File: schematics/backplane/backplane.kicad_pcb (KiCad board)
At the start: 4 copper layers, 91 x 95.3 mm, 8 parts

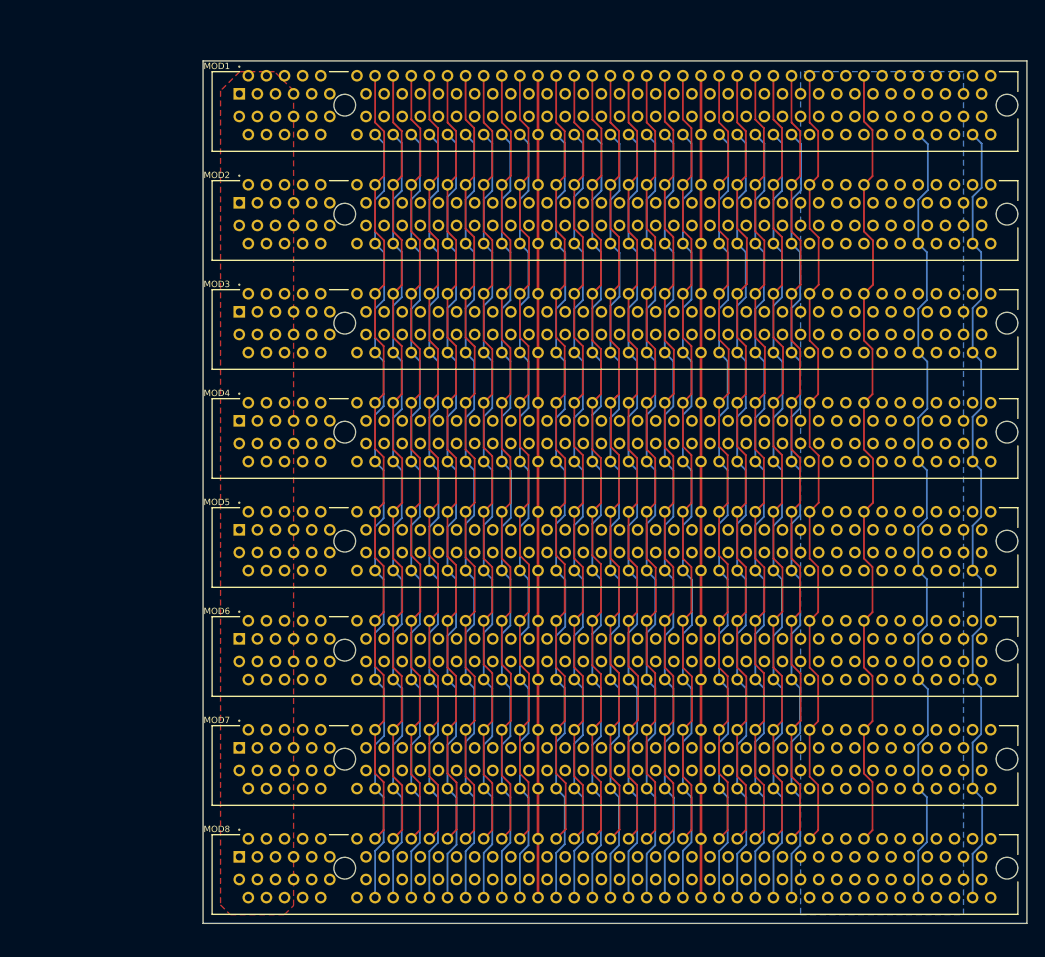
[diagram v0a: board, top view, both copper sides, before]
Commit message: Update backplane, add power supply and debug port
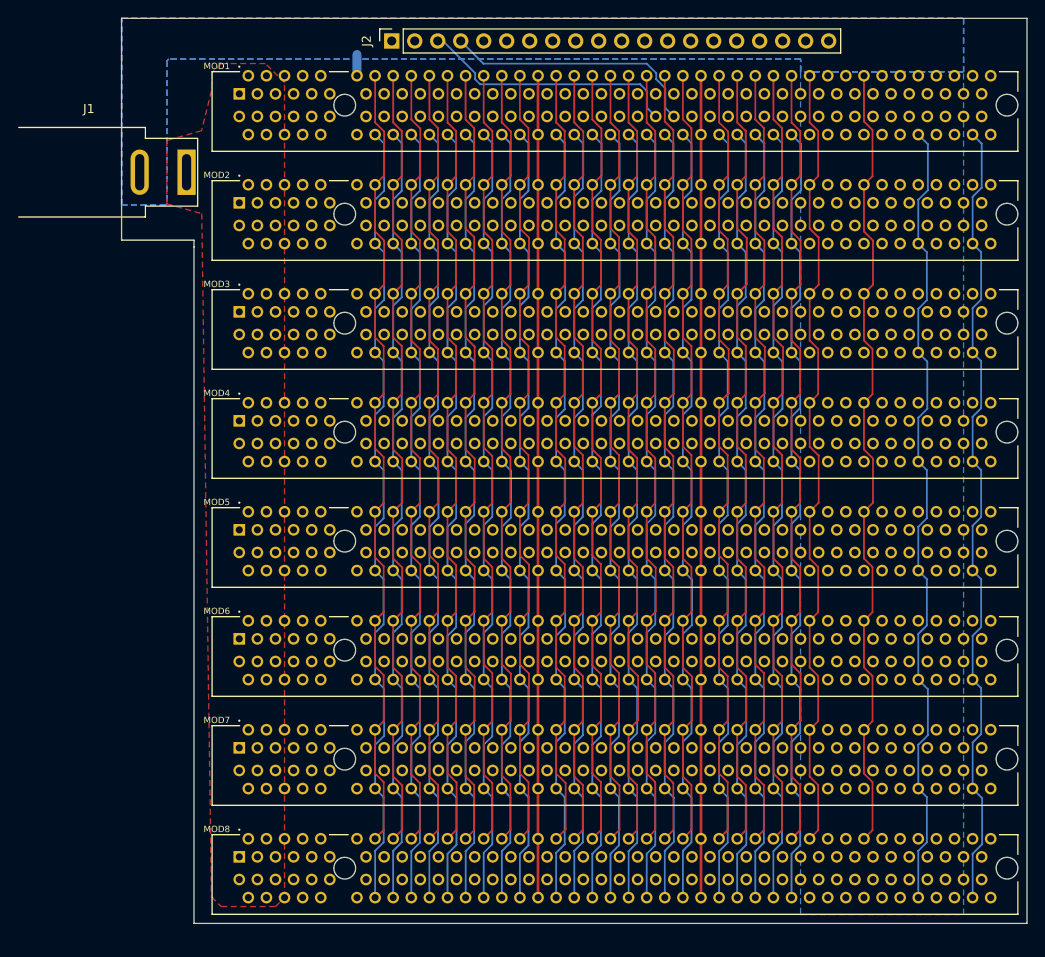
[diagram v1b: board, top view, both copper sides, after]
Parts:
- added J1: Conn_01x02, Connector_BarrelJack:BarrelJack_SwitchcraftConxall_RAPC10U_Horizontal, F.Cu at (74.2, 42.0)
- added J2: Conn_01x20, Connector_PinSocket_2.54mm:PinSocket_1x20_P2.54mm_Vertical, F.Cu at (96.8, 27.5)
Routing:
- net /~{SCCLR}: track 90.0 -> 119.0 mm
- net /PCINC: track 89.9 -> 118.6 mm
- net /STATE8: track 89.9 -> 108.9 mm
- net /STATE9: track 89.9 -> 108.1 mm
- net /STATE11: track 89.8 -> 105.0 mm
- net /STATE10: track 89.8 -> 104.3 mm
- net /STATE12: track 89.8 -> 101.2 mm
- net /STATE13: track 89.9 -> 101.3 mm
- net /STATE15: track 89.8 -> 98.2 mm
- net /STATE14: track 89.8 -> 98.2 mm
- net /DATA6: track 89.8 -> 98.1 mm
- net /DATA0: track 89.8 -> 97.8 mm
- net /DATA7: track 89.9 -> 97.6 mm
- net /DATA2: track 89.8 -> 96.3 mm
- net /DATA4: track 89.9 -> 96.3 mm
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- added copper zone on In1.Cu, net GND
- added copper zone on In2.Cu, net GND
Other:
- board size 91 x 95.3 mm -> 100 x 100 mm

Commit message: fix(backplane): changed vcc and gnd connector
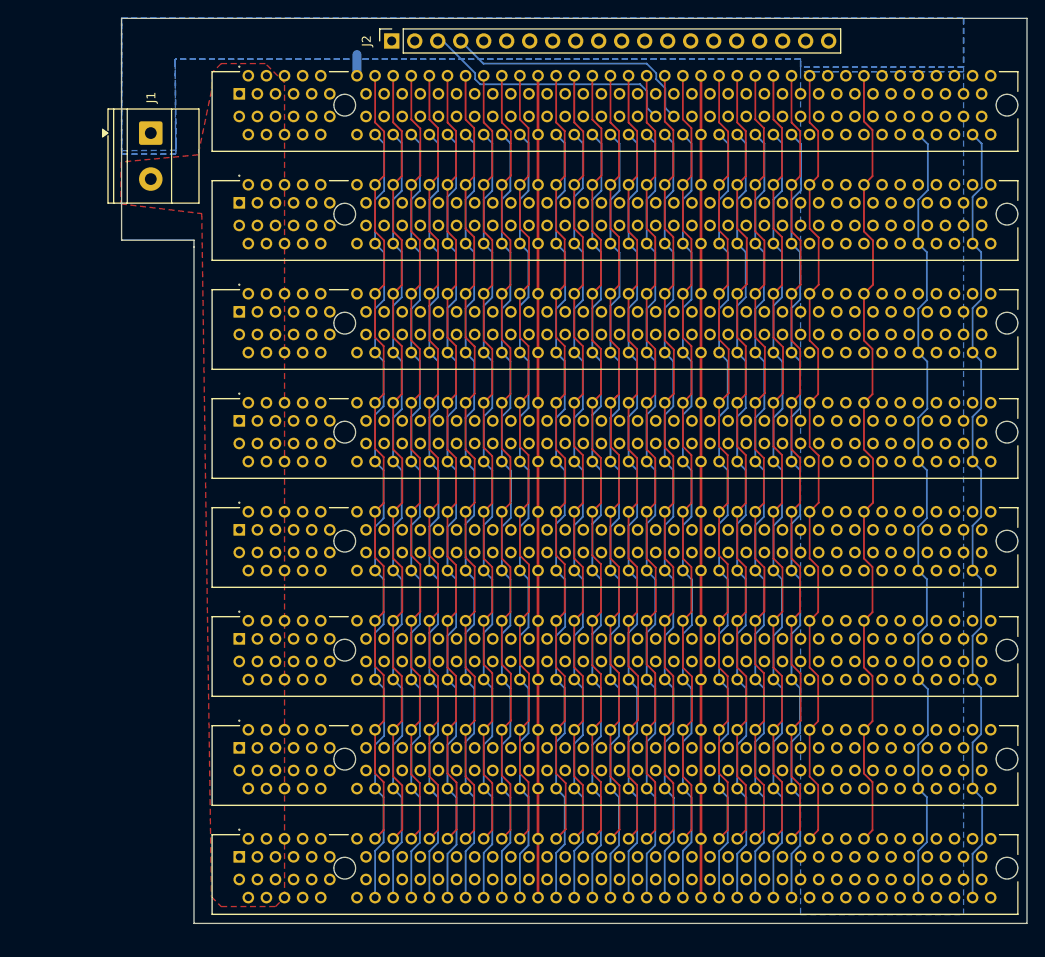
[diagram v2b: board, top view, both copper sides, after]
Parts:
- J1: value Conn_01x02 -> Screw_Terminal_01x02; footprint Connector_BarrelJack:BarrelJack_SwitchcraftConxall_RAPC10U_Horizontal -> TerminalBlock_Phoenix:TerminalBlock_Phoenix_MKDS-1,5-2-5.08_1x02_P5.08mm_Horizontal
- moved J1 5.86 mm to (70.2, 37.7), turned to -90 degrees
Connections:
- J1 pad 1: VCC -> GND
- J1 pad 2: GND -> VCC

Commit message: fix(backplane): changed connector, fixed zones issues
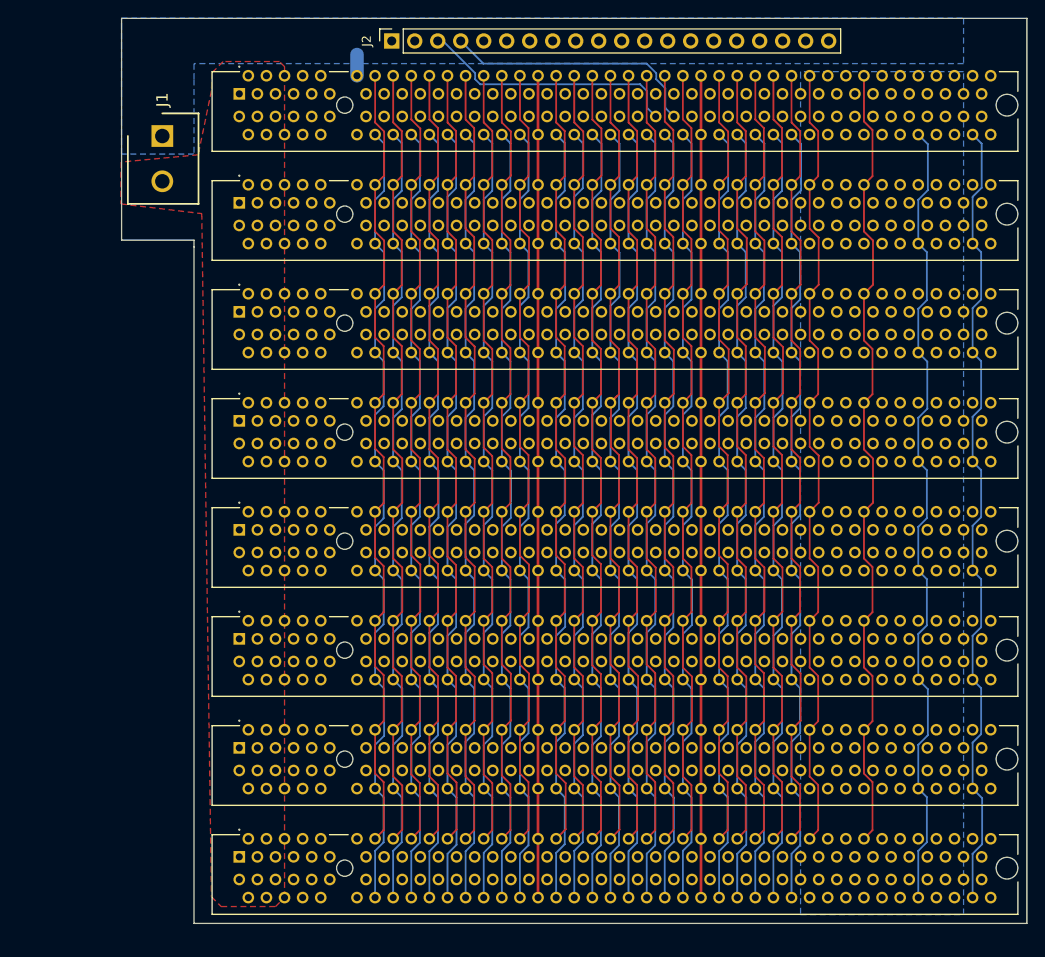
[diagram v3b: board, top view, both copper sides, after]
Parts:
- J1: footprint TerminalBlock_Phoenix:TerminalBlock_Phoenix_MKDS-1,5-2-5.08_1x02_P5.08mm_Horizontal -> TerminalBlock_Degson:SHDR2W100P0X500_1X2_1000X780X1020P
- moved J1 1.32 mm to (71.5, 38.0)

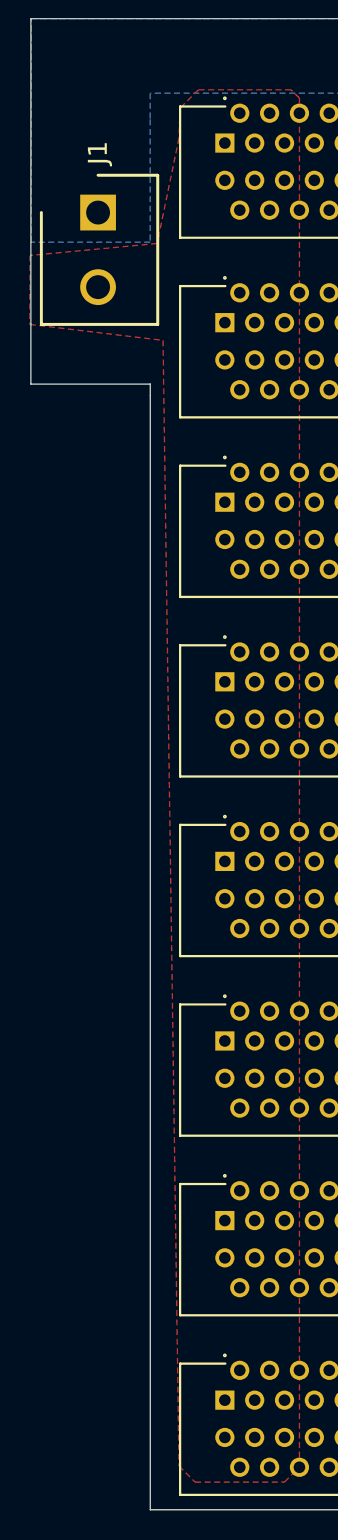
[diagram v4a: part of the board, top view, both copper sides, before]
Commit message: Add test points
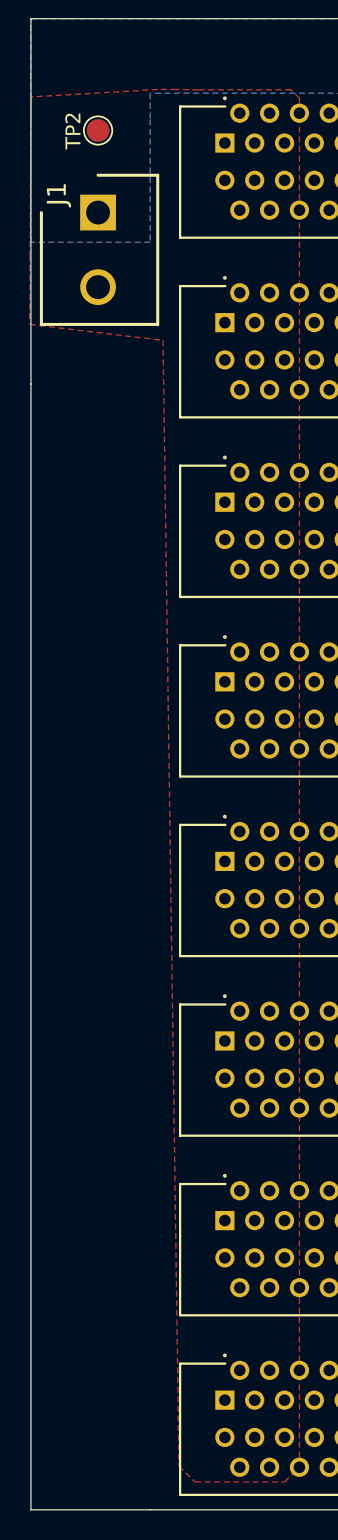
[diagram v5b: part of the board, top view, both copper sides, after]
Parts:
- added TP1: GND, TestPoint:TestPoint_Pad_D1.5mm, B.Cu at (71.5, 32.5)
- added TP2: VCC, TestPoint:TestPoint_Pad_D1.5mm, F.Cu at (71.5, 32.5)
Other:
- outline, holes or cut-outs redrawn
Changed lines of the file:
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@@
 			(size 1.8 1.8)
 			(drill 1.8)
-			(layers "F&B.Cu" "*.Mask")
+			(layers "*.Cu" "*.Mask")
 		)
 		(pad "" np_thru_hole circle
@@
 		(tags "Connector")
 		(property "Reference" "J1"
-			(at -4 0 90)
+			(at -1.25 2.75 90)
 			(layer "F.SilkS")
 			(effects
@@
 			(size 1.8 1.8)
 			(drill 1.8)
-			(layers "F&B.Cu" "*.Mask")
+			(layers "*.Cu" "*.Mask")
 		)
 		(pad "" np_thru_hole circle
@@
 			(size 1.8 1.8)
 			(drill 1.8)
-			(layers "F&B.Cu" "*.Mask")
+			(layers "*.Cu" "*.Mask")
 		)
 		(pad "" np_thru_hole circle
@@
 			(size 1.8 1.8)
 			(drill 1.8)
-			(layers "F&B.Cu" "*.Mask")
+			(layers "*.Cu" "*.Mask")
 		)
 		(pad "" np_thru_hole circle
@@
 			(size 1.8 1.8)
 			(drill 1.8)
-			(layers "F&B.Cu" "*.Mask")
+			(layers "*.Cu" "*.Mask")
 		)
 		(pad "" np_thru_hole circle
@@
 			(size 1.8 1.8)
 			(drill 1.8)
-			(layers "F&B.Cu" "*.Mask")
+			(layers "*.Cu" "*.Mask")
 		)
 		(pad "" np_thru_hole circle
@@
 			(size 1.8 1.8)
 			(drill 1.8)
-			(layers "F&B.Cu" "*.Mask")
+			(layers "*.Cu" "*.Mask")
 		)
 		(pad "" np_thru_hole circle
@@
 			(size 1.8 1.8)
 			(drill 1.8)
-			(layers "F&B.Cu" "*.Mask")
+			(layers "*.Cu" "*.Mask")
 			(zone_connect 0)
 		)
@@
 		(embedded_fonts no)
 	)
-	(gr_line
-		(start 167 25)
-		(end 67 25)
-		(stroke
-			(width 0.05)
-			(type default)
+	(footprint "TestPoint:TestPoint_Pad_D1.5mm"
+		(layer "F.Cu")
+		(at 71.5 32.5 90)
+		(descr "SMD pad as test Point, diameter 1.5mm")
+		(tags "test point SMD pad")
+		(property "Reference" "TP2"
+			(at 0 -1.648 90)
+			(layer "F.SilkS")
+			(effects
+				(font
+					(size 1 1)
+					(thickness 0.15)
+				)
+			)
 		)
-		(layer "Edge.Cuts")
+		(property "Value" "VCC"
+			(at 0 1.75 90)
+			(layer "F.Fab")
+			(effects
+				(font
+					(size 1 1)
+					(thickness 0.15)
+				)
+			)
+		)
+		(property "Datasheet" "~"
+			(at 0 0 90)
+			(unlocked yes)
+			(layer "F.Fab")
+			(hide yes)
+			(effects
+				(font
+					(size 1.27 1.27)
+					(thickness 0.15)
+				)
+			)
+		)
+		(property "Description" "test point"
+			(at 0 0 90)
+			(unlocked yes)
+			(layer "F.Fab")
+			(hide yes)
+			(effects
+				(font
+					(size 1.27 1.27)
+					(thickness 0.15)
+				)
+			)
+		)
+		(property ki_fp_filters "Pin* Test*")
+		(sheetname "/")
+		(sheetfile "backplane.kicad_sch")
+		(attr exclude_from_pos_files)
+		(fp_circle
+			(center 0 0)
+			(end 0 0.95)
+			(stroke
+				(width 0.12)
+				(type solid)
+			)
+			(fill no)
+			(layer "F.SilkS")
+		)
+		(fp_circle
+			(center 0 0)
+			(end 1.25 0)
+			(stroke
+				(width 0.05)
+				(type solid)
+			)
+			(fill no)
+			(layer "F.CrtYd")
+		)
+		(fp_text user "${REFERENCE}"
+			(at 0 -1.65 90)
+			(layer "F.Fab")
+			(effects
+				(font
+					(size 1 1)
+					(thickness 0.15)
+				)
+			)
+		)
+		(pad "1" smd circle
+			(at 0 0 90)
+			(size 1.5 1.5)
+			(layers "F.Cu" "F.Mask")
+			(net 11 "VCC")
+			(pinfunction "1")
+			(pintype "passive")
+		)
+		(embedded_fonts no)
+	)
+	(footprint "TestPoint:TestPoint_Pad_D1.5mm"
+		(layer "B.Cu")
+		(at 71.5 32.5 -90)
+		(descr "SMD pad as test Point, diameter 1.5mm")
+		(tags "test point SMD pad")
+		(property "Reference" "TP1"
+			(at 0 1.648 90)
+			(layer "B.SilkS")
+			(effects
+				(font
+					(size 1 1)
+					(thickness 0.15)
+				)
+				(justify mirror)
+			)
+		)
+		(property "Value" "GND"
+			(at 0 -1.75 90)
+			(layer "B.Fab")
+			(effects
+				(font
+					(size 1 1)
+					(thickness 0.15)
+				)
+				(justify mirror)
+			)
+		)
+		(property "Datasheet" "~"
+			(at 0 0 90)
+			(unlocked yes)
+			(layer "B.Fab")
+			(hide yes)
+			(effects
+				(font
+					(size 1.27 1.27)
+					(thickness 0.15)
+				)
+				(justify mirror)
+			)
+		)
+		(property "Description" "test point"
+			(at 0 0 90)
+			(unlocked yes)
+			(layer "B.Fab")
+			(hide yes)
+			(effects
+				(font
+					(size 1.27 1.27)
+					(thickness 0.15)
+				)
+				(justify mirror)
+			)
+		)
+		(property ki_fp_filters "Pin* Test*")
+		(sheetname "/")
+		(sheetfile "backplane.kicad_sch")
+		(attr exclude_from_pos_files)
+		(fp_circle
+			(center 0 0)
+			(end 0 -0.95)
+			(stroke
+				(width 0.12)
+				(type solid)
+			)
+			(fill no)
+			(layer "B.SilkS")
+		)
+		(fp_circle
+			(center 0 0)
+			(end 1.25 0)
+			(stroke
+				(width 0.05)
+				(type solid)
+			)
+			(fill no)
+			(layer "B.CrtYd")
+		)
+		(fp_text user "${REFERENCE}"
+			(at 0 1.65 90)
+			(layer "B.Fab")
+			(effects
+				(font
+					(size 1 1)
+					(thickness 0.15)
+				)
+				(justify mirror)
+			)
+		)
+		(pad "1" smd circle
+			(at 0 0 270)
+			(size 1.5 1.5)
+			(layers "B.Cu" "B.Mask")
+			(net 5 "GND")
+			(pinfunction "1")
+			(pintype "passive")
+		)
+		(embedded_fonts no)
 	)
 	(gr_line
 		(start 75 124.97)
-		(end 75 50.25)
+		(end 67 124.97)
 		(stroke
 			(width 0.05)
@@
 	)
 	(gr_line
-		(start 67 49.5)
-		(end 75 49.5)
+		(start 167 25)
+		(end 67 25)
 		(stroke
 			(width 0.05)
@@
 	)
 	(gr_line
-		(start 167 124.97)
-		(end 167 25)
+		(start 67 49.5)
+		(end 67 124.97)
 		(stroke
 			(width 0.05)
@@
 	)
 	(gr_line
-		(start 67 25)
-		(end 67 49.5)
+		(start 167 124.97)
+		(end 167 25)
 		(stroke
 			(width 0.05)
@@
 	)
 	(gr_line
-		(start 75 50.25)
-		(end 75 49.5)
+		(start 67 25)
+		(end 67 49.5)
 		(stroke
 			(width 0.05)
@@
 		(polygon
 			(pts
-				(xy 78.23 29.77) (xy 77 31) (xy 76.926 33) (xy 75.459468 40.075) (xy 66.943506 40.875) (xy 66.925 45.5)
+				(xy 78.23 29.77) (xy 76.75 29.75) (xy 75.5 29.75) (xy 67 30.25) (xy 66.943506 40.875) (xy 66.925 45.5)
 				(xy 75.85639 46.56961) (xy 76.926 122.036) (xy 78 123.11) (xy 84 123.11) (xy 85 122.11) (xy 85 30.33)
 				(xy 84.44 29.77)

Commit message: Add signatures
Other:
- board text added: "ANDRII KRYVYI"
- board text added: "ANDRII MOROZ"
- board text added: "LUKA KONOVALOV"
- board text added: "MADE BY"
- board text added: "NIKITA LENYK"
- board text added: "OSTAP KOSTIUK"
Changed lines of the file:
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@@
 		(layer "Edge.Cuts")
+	)
+	(gr_text "NIKITA LENYK"
+		(at 74 103 90)
+		(layer "F.SilkS")
+		(effects
+			(font
+				(size 1.5 1.5)
+				(thickness 0.3)
+				(bold yes)
+			)
+			(justify left bottom)
+		)
+	)
+	(gr_text "ANDRII MOROZ"
+		(at 72.5 63 90)
+		(layer "F.SilkS")
+		(effects
+			(font
+				(size 1.5 1.5)
+				(thickness 0.3)
+				(bold yes)
+			)
+			(justify left bottom)
+		)
+	)
+	(gr_text "MADE BY"
+		(at 73 114.5 90)
+		(layer "F.SilkS")
+		(effects
+			(font
+				(size 3 3)
+				(thickness 0.3)
+				(bold yes)
+			)
+			(justify bottom)
+		)
+	)
+	(gr_text "ANDRII KRYVYI"
+		(at 70.25 103 90)
+		(layer "F.SilkS")
+		(effects
+			(font
+				(size 1.5 1.5)
+				(thickness 0.3)
+				(bold yes)
+			)
+			(justify left bottom)
+		)
+	)
+	(gr_text "OSTAP KOSTIUK"
+		(at 74 84.5 90)
+		(layer "F.SilkS")
+		(effects
+			(font
+				(size 1.5 1.5)
+				(thickness 0.3)
+				(bold yes)
+			)
+			(justify left bottom)
+		)
+	)
+	(gr_text "LUKA KONOVALOV"
+		(at 70.25 84.5 90)
+		(layer "F.SilkS")
+		(effects
+			(font
+				(size 1.5 1.5)
+				(thickness 0.3)
+				(bold yes)
+			)
+			(justify left bottom)
+		)
 	)
 	(segment
